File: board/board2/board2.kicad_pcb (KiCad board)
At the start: 2 copper layers, 25.4 x 39.5 mm, 7 parts, among them J1 11-PIN HDR, J2 MITSU_AC, J3 11-PIN HDR, U1 TXB0104D

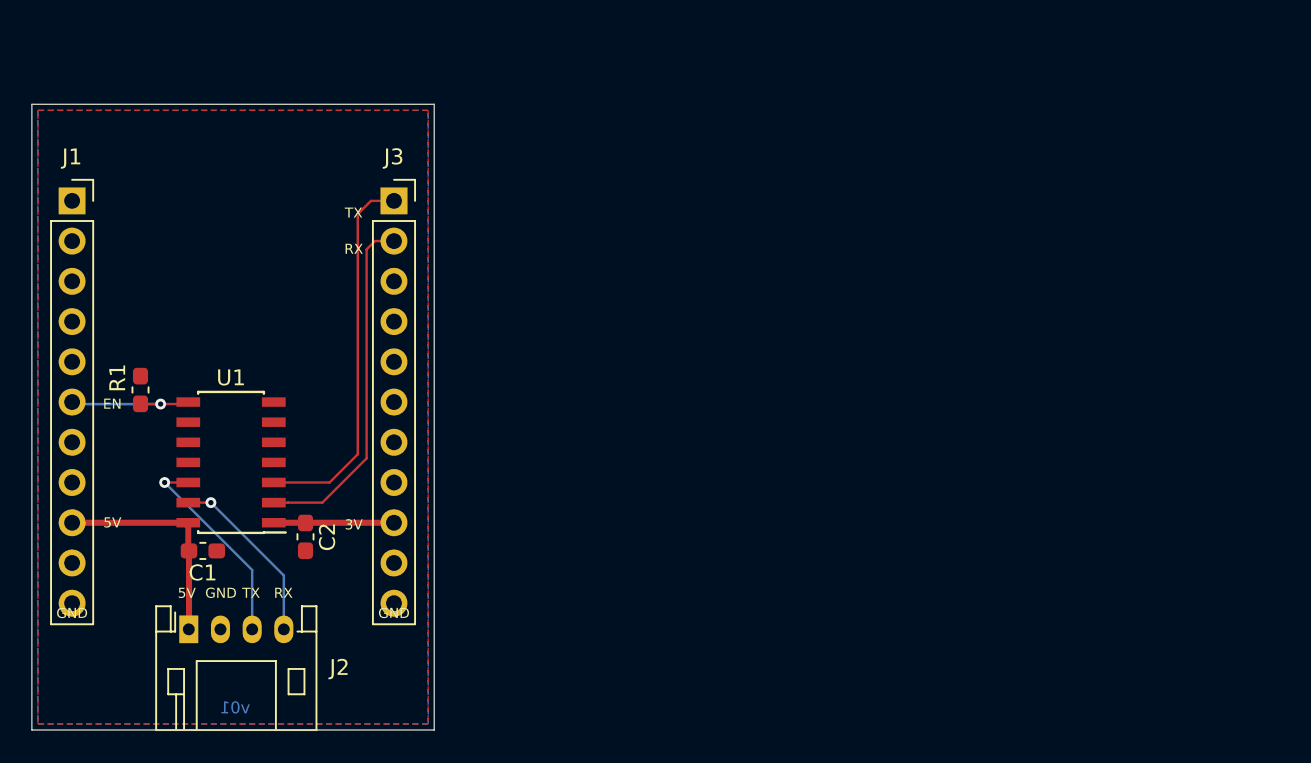
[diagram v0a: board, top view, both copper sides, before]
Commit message: Commit the old board changes for posterity
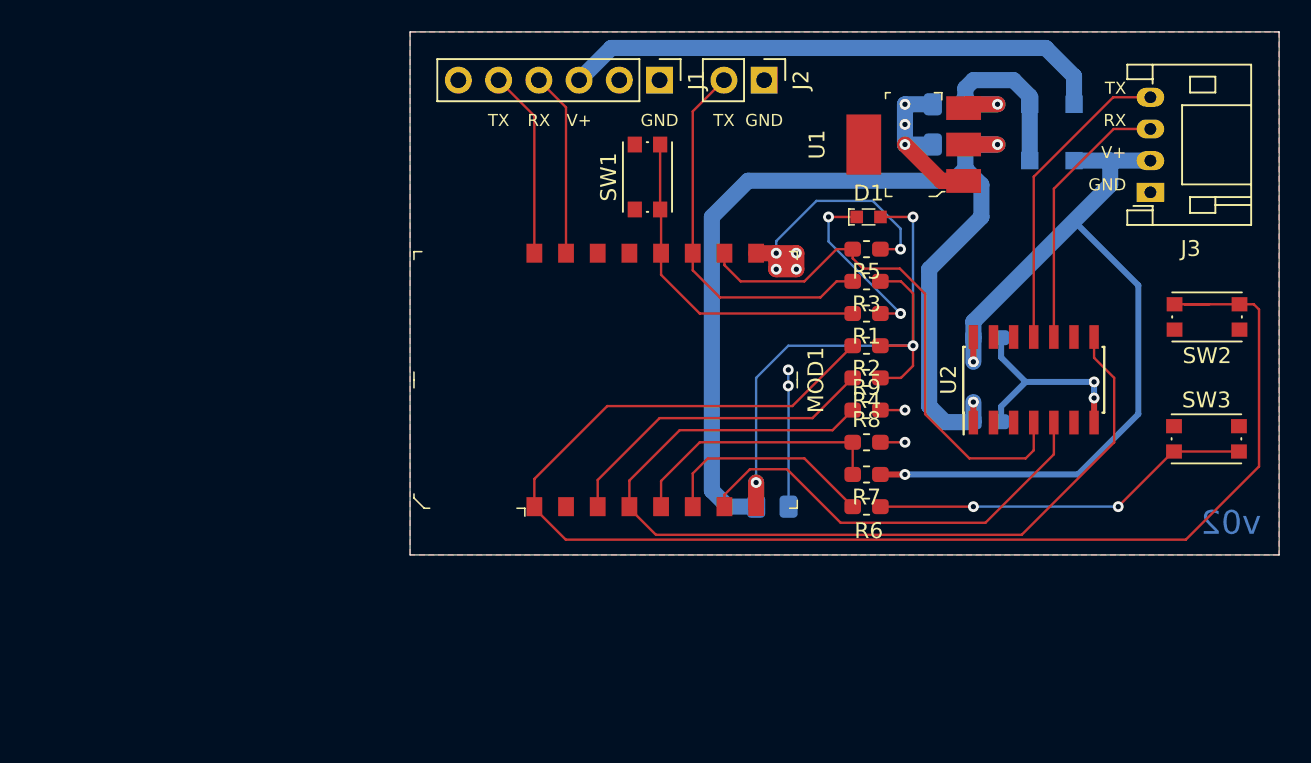
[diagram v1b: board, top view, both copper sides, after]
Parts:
- added C3: 10uF, Capacitor_SMD:C_0805_2012Metric_Pad1.15x1.40mm_HandSolder, B.Cu at (163.6, 104.1)
- added C4: 0.1uF, Capacitor_SMD:C_0603_1608Metric_Pad1.05x0.95mm_HandSolder, B.Cu at (177.2, 93.5)
- added C5: 0.1uF, Capacitor_SMD:C_0603_1608Metric_Pad1.05x0.95mm_HandSolder, B.Cu at (177.2, 98.8)
- added D1: RED, digikey-footprints:LED_2-SMD_No_Lead_1.7x0.8mm, F.Cu at (169.7, 85.9)
- added D2: D_Schottky, Diode_SMD:D_SOD-123F, B.Cu at (181.2, 78.7)
- added D3: D_Schottky, Diode_SMD:D_SOD-123F, B.Cu at (181.2, 82.3)
- added MOD1: ESP-12S, digikey-footprints:WIFI_Module_ESP8266_2491, F.Cu at (155.6, 96.1)
- added R2: 10K, Resistor_SMD:R_0603_1608Metric_Pad1.05x0.95mm_HandSolder, F.Cu at (169.5, 94.0)
- added R3: 10K, Resistor_SMD:R_0603_1608Metric_Pad1.05x0.95mm_HandSolder, F.Cu at (169.5, 89.9)
- added R4: 10K, Resistor_SMD:R_0603_1608Metric_Pad1.05x0.95mm_HandSolder, F.Cu at (169.5, 96.0)
- added R5: 10K, Resistor_SMD:R_0603_1608Metric_Pad1.05x0.95mm_HandSolder, F.Cu at (169.5, 87.9)
- added R6: 10K, Resistor_SMD:R_0603_1608Metric_Pad1.05x0.95mm_HandSolder, F.Cu at (169.5, 104.1)
- added R7: 1K8, Resistor_SMD:R_0603_1608Metric_Pad1.05x0.95mm_HandSolder, F.Cu at (169.5, 102.1)
- added R8: 3K3, Resistor_SMD:R_0603_1608Metric_Pad1.05x0.95mm_HandSolder, F.Cu at (169.5, 100.1)
- added R9: 10K, Resistor_SMD:R_0603_1608Metric_Pad1.05x0.95mm_HandSolder, F.Cu at (169.5, 98.0)
- added SW1: SW_Push, Button_Switch_SMD:SW_SPST_KMR2, F.Cu at (155.7, 83.3)
- added SW2: SW_Push, Button_Switch_SMD:SW_SPST_KMR2, F.Cu at (191.0, 92.2)
- added SW3: SW_Push, Button_Switch_SMD:SW_SPST_KMR2, F.Cu at (191.0, 99.9)
- added U2: TXB0104D, Package_SO:SOIC-14_3.9x8.7mm_P1.27mm, F.Cu at (180.1, 96.1)
- C1, C2: value 0.1uF -> 10uF; footprint Capacitor_SMD:C_0603_1608Metric_Pad1.05x0.95mm_HandSolder -> Capacitor_SMD:C_0805_2012Metric_Pad1.15x1.40mm_HandSolder; moved to B.Cu
- J1: value 11-PIN HDR -> FTDI; footprint Connector_PinSocket_2.54mm:PinSocket_1x11_P2.54mm_Vertical -> Connector_PinHeader_2.54mm:PinHeader_1x06_P2.54mm_Vertical
- J2: value MITSU_AC -> DEBUG; footprint Connector_JST:JST_PH_S4B-PH-K_1x04_P2.00mm_Horizontal -> Connector_PinHeader_2.54mm:PinHeader_1x02_P2.54mm_Vertical
- J3: value 11-PIN HDR -> MITSU_AC; footprint Connector_PinSocket_2.54mm:PinSocket_1x11_P2.54mm_Vertical -> Connector_JST:JST_PH_S4B-PH-K_1x04_P2.00mm_Horizontal
- R1: value 10K -> 1K
- U1: value TXB0104D -> AP2114H-3_3TRG1; footprint Package_SO:SOIC-14_3.9x8.7mm_P1.27mm -> digikey-footprints:SOT-223
- moved C1 54.9 mm to (174.7, 78.7), turned to 180 degrees
- moved J2 50.2 mm to (163.1, 77.2), turned to 270 degrees
- moved J3 47.8 mm to (187.5, 84.3), turned to 90 degrees
- moved C2 47.6 mm to (174.7, 81.3), turned to 180 degrees
- moved U1 47.5 mm to (172.5, 81.3), turned to 90 degrees
- moved R1 46.1 mm to (169.5, 91.9), turned to 180 degrees
- moved J1 37.9 mm to (156.5, 77.2), turned to 270 degrees
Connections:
- C1 pad 1: +5V -> VCC
- J1 pad 1: Net-(J1-Pad1) -> GND
- J1 pad 3: Net-(J1-Pad3) -> VPP
- J1 pad 4: Net-(J1-Pad4) -> /RX0
- J1 pad 5: Net-(J1-Pad5) -> /TX0
- J1 pad 6: /EN -> Net-(J1-Pad6)
- J2 pad 1: +5V -> GND
- J2 pad 2: GND -> /GPIO2
- J3 pad 1: /TX0 -> GND
- J3 pad 2: /RX0 -> VBUS
- J3 pad 3: Net-(J3-Pad3) -> /RX0*_5V
- J3 pad 4: Net-(J3-Pad4) -> /TX0*_5V
- R1 pad 1: /EN -> Net-(D1-Pad1)
- R1 pad 2: GND -> /GPIO0
- U1 pad 1: +3V3 -> GND
- U1 pad 2: /RX0 -> +3V3
- U1 pad 3: /TX0 -> VCC
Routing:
- net +3V3: track 7.78 -> 108.0 mm, vias 0 -> 5
- net /RESET: track 0.00 -> 90.8 mm
- net /GPIO16: track 0.00 -> 58.6 mm
- net GND: track 0.00 -> 54.7 mm, vias 0 -> 14
- net VBUS: track 0.00 -> 54.4 mm, vias 0 -> 2
- net VPP: track 0.00 -> 34.6 mm
- net /GPIO15: track 0.00 -> 33.8 mm
- net /GPIO13: track 0.00 -> 27.4 mm
- net Net-(R6-Pad2): track 0.00 -> 24.1 mm, vias 0 -> 2
- net /GPIO2: track 0.00 -> 24.0 mm
- net /GPIO0: track 0.00 -> 21.4 mm
- net /CH_PD: track 0.00 -> 20.4 mm
- net /TX0*_5V: track 0.00 -> 19.6 mm
- net /RX0*_5V: track 0.00 -> 17.0 mm
- net /GPIO14: track 0.00 -> 16.8 mm
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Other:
- board size 25.4 x 39.5 mm -> 54.9 x 33 mm
- board text added: "V+"
- board text added: "v02"
- board text removed: "3V"
- board text removed: "5V"
- board text removed: "EN"
- board text removed: "HUZZAH"
- board text removed: "Mitsu.AC"
- board text removed: "v01"
- board text removed: "x"
